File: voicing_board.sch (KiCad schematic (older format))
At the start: 275 parts, among them Q1 MMBT3904, Q14 MMBT3904, Q15 MMBT3904, Q16 MMBT3904, Q17 MMBT3904, Q18 MMBT3904, Q19 MMBT3904, Q2 MMBT3904, Q20 MMBT3904, Q21 MMBT3904, Q22 MMBT3904, Q23 MMBT3904, Q24 MMBT3904, Q25 MMBT3904, Q26 MMBT3904, Q27 MMBT3904, Q28-1 MMBT3904, Q29-1 MMBT3904, Q3 MMBT3904, Q30 MMBT3904, Q31-1 MMBT3904, Q4 MMBT3904, Q5 MMBT3906, Q6 MMBT3906, Q7 MMBT3906, Q8 MMBT3906, Q9 MMBT3904, U1 MC14584, U2 4558, U3 4558, U5 4558, U6-1 4558, U7 4558

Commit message: first commit since importing netlist with updated footprints. Bit of a mess now. Major reroute is in order
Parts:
- C35, C61-1: footprint Capacitors_SMD:c_elec_6.3x5.3 -> Capacitors_SMD:c_elec_5x5.3
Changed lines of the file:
@@
 F 0 "C35" H 9450 9475 50  0000 L CNN
 F 1 "47μ" H 9750 9475 50  0000 L CNN
-F 2 "Capacitors_SMD:c_elec_6.3x5.3" H 9675 9575 60  0001 C CNN
+F 2 "Capacitors_SMD:c_elec_5x5.3" H 9675 9575 60  0001 C CNN
 F 3 "" H 9675 9575 60  0000 C CNN
 	1    9675 9575
@@
 F 0 "C61-1" H 13175 2575 50  0000 L CNN
 F 1 "47μ" H 13175 2500 50  0000 L CNN
-F 2 "Capacitors_SMD:c_elec_6.3x5.3" H 13050 2550 60  0001 C CNN
+F 2 "Capacitors_SMD:c_elec_5x5.3" H 13050 2550 60  0001 C CNN
 F 3 "" H 13050 2550 60  0000 C CNN
 	1    13050 2550

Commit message: epic pcb overhaul for 2.0 has begun. depressing
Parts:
- removed TP22, TP23, TP24, TP25: TEST_POINT, MyModules:TEST_POINT_LOOP_4592, symbol TEST_POINT
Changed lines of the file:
@@
 Text HLabel 1775 750  0    100  Input ~ 0
 COMMON_TRIG
-Text HLabel 1450 3600 0    100  Input ~ 0
+Text HLabel 1450 3500 0    100  Input ~ 0
 CB_TRIG
 Text HLabel 12050 7025 2    100  Output ~ 0
@@
 $EndComp
 $Comp
-L R_US R2-1
-U 1 1 56A1AAD0
-P 7825 2325
-F 0 "R2-1" H 7675 2350 50  0000 C CNN
-F 1 "22K" H 7700 2250 50  0000 C CNN
-F 2 "MyModules:SM0603-R-JRL" H 7825 2325 60  0001 C CNN
-F 3 "" H 7825 2325 60  0000 C CNN
-	1    7825 2325
-	1    0    0    -1
-$EndComp
-$Comp
 L R_US R7-1
 U 1 1 56A1AAD6
@@
 	-1   0    0    1
 $EndComp
-Text HLabel 7675 2125 0    100  Input ~ 0
+Text HLabel 7675 2025 0    100  Input ~ 0
 CH_TRIG
 $Comp
@@
 	-1   0    0    1
 $EndComp
-Text HLabel 9700 2125 0    100  Input ~ 0
+Text HLabel 9700 2025 0    100  Input ~ 0
 OH_TRIG
 $Comp
@@
 	1600 4850 1600 4925
 Connection ~ 1600 4425
-Wire Wire Line
-	1450 3600 1600 3600
 Connection ~ 2075 2800
 Wire Wire Line
@@
 	7825 3375 7825 3450
 Connection ~ 7825 2950
-Wire Wire Line
-	7675 2125 7825 2125
 Connection ~ 8300 1325
 Wire Wire Line
@@
 	9850 3375 9850 3450
 Connection ~ 9850 2950
-Wire Wire Line
-	9700 2125 9850 2125
 Connection ~ 10325 1325
 Wire Wire Line
@@
 	0    1    1    0
 $EndComp
-$Comp
-L TEST_POINT TP22
-U 1 1 56CCF221
-P 1600 3450
-F 0 "TP22" V 1750 3275 100 0000 L CNB
-F 1 "TEST_POINT" H 1600 3505 30  0001 C CNN
-F 2 "MyModules:TEST_POINT_LOOP_4592" H 1600 3450 60  0001 C CNN
-F 3 "" H 1600 3450 60  0000 C CNN
-	1    1600 3450
-	0    -1   -1   0
-$EndComp
-Connection ~ 1600 3600
-$Comp
-L TEST_POINT TP23
-U 1 1 56CD43FC
-P 7825 1975
-F 0 "TP23" V 7825 1600 100 0000 L CNB
-F 1 "TEST_POINT" H 7825 2030 30  0001 C CNN
-F 2 "MyModules:TEST_POINT_LOOP_4592" H 7825 1975 60  0001 C CNN
-F 3 "" H 7825 1975 60  0000 C CNN
-	1    7825 1975
-	0    -1   -1   0
-$EndComp
-$Comp
-L TEST_POINT TP24
-U 1 1 56CD66B0
-P 9850 1975
-F 0 "TP24" V 9850 1600 100 0000 L CNB
-F 1 "TEST_POINT" H 9850 2030 30  0001 C CNN
-F 2 "MyModules:TEST_POINT_LOOP_4592" H 9850 1975 60  0001 C CNN
-F 3 "" H 9850 1975 60  0000 C CNN
-	1    9850 1975
-	0    -1   -1   0
-$EndComp
-Connection ~ 9850 2125
-Connection ~ 7825 2125
-$Comp
-L TEST_POINT TP25
-U 1 1 56CD9E51
-P 13350 8875
-F 0 "TP25" V 13350 8500 100 0000 L CNB
-F 1 "TEST_POINT" H 13350 8930 30  0001 C CNN
-F 2 "MyModules:TEST_POINT_LOOP_4592" H 13350 8875 60  0001 C CNN
-F 3 "" H 13350 8875 60  0000 C CNN
-	1    13350 8875
-	0    -1   -1   0
-$EndComp
-Connection ~ 13350 9025
 Connection ~ 19150 5850
 NoConn ~ 1600 6875
@@
 Text Notes 9750 3750 0    60   ~ 0
 Simulate this OH decay circuit!
+$Comp
+L R_US R2-1
+U 1 1 56A1AAD0
+P 7825 2325
+F 0 "R2-1" H 7675 2350 50  0000 C CNN
+F 1 "22K" H 7700 2250 50  0000 C CNN
+F 2 "MyModules:SM0603-R-JRL" H 7825 2325 60  0001 C CNN
+F 3 "" H 7825 2325 60  0000 C CNN
+	1    7825 2325
+	1    0    0    -1
+$EndComp
+Wire Wire Line
+	7675 2025 7825 2025
+Wire Wire Line
+	7825 2025 7825 2125
+Wire Wire Line
+	9700 2025 9850 2025
+Wire Wire Line
+	9850 2025 9850 2125
+Wire Wire Line
+	1450 3500 1600 3500
+Wire Wire Line
+	1600 3500 1600 3600
 $EndSCHEMATC

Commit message: changed all NPN and PNPs to 945 and 733 respectively
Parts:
- Q1, Q14, Q15, Q16, Q17, Q18, Q19, Q2, Q20, Q21, Q22, Q23, Q24, Q25, Q26, Q27, Q28-1, Q29-1, Q3, Q30, Q31-1, Q4, Q9: value MMBT3904 -> C945; symbol MMBT3904 -> C945
- Q5, Q6, Q7, Q8: value MMBT3906 -> A733; symbol MMBT3906 -> A733
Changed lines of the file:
@@
 $EndComp
 $Comp
-L MMBT3904 Q9
+L C945 Q9
 U 1 1 5693E26E
 P 1850 5950
 F 0 "Q9" H 2075 6150 100 0000 L CNB
-F 1 "MMBT3904" H 1450 5825 50  0001 L CNN
+F 1 "C945" H 1450 5825 50  0001 L CNN
 F 2 "MyModules:SOT23-132-JRL" H 2050 5875 50  0001 L CIN
 F 3 "" H 1850 5950 50  0000 L CNN
@@
 $EndComp
 $Comp
-L MMBT3904 Q15
+L C945 Q15
 U 1 1 5693E2F3
 P 4725 5825
 F 0 "Q15" H 4675 6200 100 0000 L CNB
-F 1 "MMBT3904" H 4325 5700 50  0001 L CNN
+F 1 "C945" H 4325 5700 50  0001 L CNN
 F 2 "MyModules:SOT23-132-JRL" H 4925 5750 50  0001 L CIN
 F 3 "" H 4725 5825 50  0000 L CNN
@@
 $EndComp
 $Comp
-L MMBT3904 Q14
+L C945 Q14
 U 1 1 5693E468
 P 4775 7225
 F 0 "Q14" H 4775 7600 100 0000 L CNB
-F 1 "MMBT3904" H 4375 7100 50  0001 L CNN
+F 1 "C945" H 4375 7100 50  0001 L CNN
 F 2 "MyModules:SOT23-132-JRL" H 4975 7150 50  0001 L CIN
 F 3 "" H 4775 7225 50  0000 L CNN
@@
 CB\nLEVEL
 $Comp
-L MMBT3904 Q1
+L C945 Q1
 U 1 1 5693E582
 P 1975 4425
 F 0 "Q1" H 1800 4675 100 0000 L CNB
-F 1 "MMBT3904" H 1650 4650 50  0001 L CNN
+F 1 "C945" H 1650 4650 50  0001 L CNN
 F 2 "MyModules:SOT23-132-JRL" H 2175 4350 50  0001 L CIN
 F 3 "" H 1975 4425 50  0000 L CNN
@@
 $EndComp
 $Comp
-L MMBT3906 Q5
+L A733 Q5
 U 1 1 5693E589
 P 2375 3425
 F 0 "Q5" H 2575 3225 100 0000 L CNB
-F 1 "MMBT3906" H 2575 3425 50  0001 L CNN
+F 1 "A733" H 2575 3425 50  0001 L CNN
 F 2 "MyModules:SOT23-132-JRL" H 2575 3350 50  0001 L CIN
 F 3 "" H 2375 3425 50  0000 L CNN
@@
 $EndComp
 $Comp
-L MMBT3904 Q17
+L C945 Q17
 U 1 1 5693E686
 P 6125 11800
 F 0 "Q17" H 5800 11525 100 0000 L CNB
-F 1 "MMBT3904" H 5725 11675 50  0001 L CNN
+F 1 "C945" H 5725 11675 50  0001 L CNN
 F 2 "MyModules:SOT23-132-JRL" H 6325 11725 50  0001 L CIN
 F 3 "" H 6125 11800 50  0000 L CNN
@@
 $EndComp
 $Comp
-L MMBT3904 Q16
+L C945 Q16
 U 1 1 5693E6ED
 P 6125 9125
 F 0 "Q16" H 5825 8900 100 0000 L CNB
-F 1 "MMBT3904" H 5725 9000 50  0001 L CNN
+F 1 "C945" H 5725 9000 50  0001 L CNN
 F 2 "MyModules:SOT23-132-JRL" H 6325 9050 50  0001 L CIN
 F 3 "" H 6125 9125 50  0000 L CNN
@@
 $EndComp
 $Comp
-L MMBT3904 Q19
+L C945 Q19
 U 1 1 5693E7B7
 P 10400 9825
 F 0 "Q19" H 10100 9625 100 0000 L CNB
-F 1 "MMBT3904" H 10000 9700 50  0001 L CNN
+F 1 "C945" H 10000 9700 50  0001 L CNN
 F 2 "MyModules:SOT23-132-JRL" H 10600 9750 50  0001 L CIN
 F 3 "" H 10400 9825 50  0000 L CNN
@@
 $EndComp
 $Comp
-L MMBT3904 Q20
+L C945 Q20
 U 1 1 5693E7F3
 P 8550 12325
 F 0 "Q20" H 8275 12550 100 0000 L CNB
-F 1 "MMBT3904" H 8150 12200 50  0001 L CNN
+F 1 "C945" H 8150 12200 50  0001 L CNN
 F 2 "MyModules:SOT23-132-JRL" H 8750 12250 50  0001 L CIN
 F 3 "" H 8550 12325 50  0000 L CNN
@@
 $EndComp
 $Comp
-L MMBT3904 Q25
+L C945 Q25
 U 1 1 569A0C3C
 P 8925 14250
 F 0 "Q25" H 9125 14350 100 0000 L CNB
-F 1 "MMBT3904" H 8525 14125 50  0001 L CNN
+F 1 "C945" H 8525 14125 50  0001 L CNN
 F 2 "MyModules:SOT23-132-JRL" H 9125 14175 50  0001 L CIN
 F 3 "" H 8925 14250 50  0000 L CNN
@@
 $EndComp
 $Comp
-L MMBT3904 Q18
+L C945 Q18
 U 1 1 569A4928
 P 6125 14450
 F 0 "Q18" H 6100 14750 100 0000 L CNB
-F 1 "MMBT3904" H 5725 14325 50  0001 L CNN
+F 1 "C945" H 5725 14325 50  0001 L CNN
 F 2 "MyModules:SOT23-132-JRL" H 6325 14375 50  0001 L CIN
 F 3 "" H 6125 14450 50  0000 L CNN
@@
 CY\nLEVEL
 $Comp
-L MMBT3904 Q2
+L C945 Q2
 U 1 1 569FC4C8
 P 12975 9700
 F 0 "Q2" H 12800 9925 100 0000 L CNB
-F 1 "MMBT3904" H 12650 9925 50  0001 L CNN
+F 1 "C945" H 12650 9925 50  0001 L CNN
 F 2 "MyModules:SOT23-132-JRL" H 13175 9625 50  0001 L CIN
 F 3 "" H 12975 9700 50  0000 L CNN
@@
 $EndComp
 $Comp
-L MMBT3906 Q6
+L A733 Q6
 U 1 1 569FC4CE
 P 12575 8850
 F 0 "Q6" H 12775 8925 100 0000 L CNB
-F 1 "MMBT3906" H 12775 8850 50  0001 L CNN
+F 1 "A733" H 12775 8850 50  0001 L CNN
 F 2 "MyModules:SOT23-132-JRL" H 12775 8775 50  0001 L CIN
 F 3 "" H 12575 8850 50  0000 L CNN
@@
 $EndComp
 $Comp
-L MMBT3904 Q4
+L C945 Q4
 U 1 1 56A1AAB2
 P 8200 2950
 F 0 "Q4" H 8050 2650 100 0000 L CNB
-F 1 "MMBT3904" H 7875 3175 50  0001 L CNN
+F 1 "C945" H 7875 3175 50  0001 L CNN
 F 2 "MyModules:SOT23-132-JRL" H 8400 2875 50  0001 L CIN
 F 3 "" H 8200 2950 50  0000 L CNN
@@
 $EndComp
 $Comp
-L MMBT3906 Q8
+L A733 Q8
 U 1 1 56A1AAB8
 P 8600 1950
 F 0 "Q8" H 8800 1700 100 0000 L CNB
-F 1 "MMBT3906" H 8800 1950 50  0001 L CNN
+F 1 "A733" H 8800 1950 50  0001 L CNN
 F 2 "MyModules:SOT23-132-JRL" H 8800 1875 50  0001 L CIN
 F 3 "" H 8600 1950 50  0000 L CNN
@@
 CH_TRIG
 $Comp
-L MMBT3904 Q3
+L C945 Q3
 U 1 1 56A1B851
 P 10225 2950
 F 0 "Q3" H 10050 2725 100 0000 L CNB
-F 1 "MMBT3904" H 9900 3175 50  0001 L CNN
+F 1 "C945" H 9900 3175 50  0001 L CNN
 F 2 "MyModules:SOT23-132-JRL" H 10425 2875 50  0001 L CIN
 F 3 "" H 10225 2950 50  0000 L CNN
@@
 $EndComp
 $Comp
-L MMBT3906 Q7
+L A733 Q7
 U 1 1 56A1B857
 P 10775 1950
 F 0 "Q7" H 10975 1700 100 0000 L CNB
-F 1 "MMBT3906" H 10975 1950 50  0001 L CNN
+F 1 "A733" H 10975 1950 50  0001 L CNN
 F 2 "MyModules:SOT23-132-JRL" H 10975 1875 50  0001 L CIN
 F 3 "" H 10775 1950 50  0000 L CNN
@@
 $EndComp
 $Comp
-L MMBT3904 Q21
+L C945 Q21
 U 1 1 56A27D2F
 P 10425 4300
 F 0 "Q21" H 10650 4175 100 0000 L CNB
-F 1 "MMBT3904" H 10600 4225 50  0001 L CNN
+F 1 "C945" H 10600 4225 50  0001 L CNN
 F 2 "MyModules:SOT23-132-JRL" H 10625 4225 50  0001 L CIN
 F 3 "" H 10425 4300 50  0000 L CNN
@@
 $EndComp
 $Comp
-L MMBT3904 Q24
+L C945 Q24
 U 1 1 56A41564
 P 11700 2825
 F 0 "Q24" H 11875 3025 100 0000 L CNB
-F 1 "MMBT3904" H 11375 3050 50  0001 L CNN
+F 1 "C945" H 11375 3050 50  0001 L CNN
 F 2 "MyModules:SOT23-132-JRL" H 11900 2750 50  0001 L CIN
 F 3 "" H 11700 2825 50  0000 L CNN
@@
 $EndComp
 $Comp
-L MMBT3904 Q29-1
+L C945 Q29-1
 U 1 1 56A4ABB0
 P 13600 3075
 F 0 "Q29-1" H 13125 2850 100 0000 L CNB
-F 1 "MMBT3904" H 13275 3300 50  0001 L CNN
+F 1 "C945" H 13275 3300 50  0001 L CNN
 F 2 "MyModules:SOT23-132-JRL" H 13800 3000 50  0001 L CIN
 F 3 "" H 13600 3075 50  0000 L CNN
@@
 $EndComp
 $Comp
-L MMBT3904 Q28-1
+L C945 Q28-1
 U 1 1 56A59C33
 P 13600 4875
 F 0 "Q28-1" H 13500 5325 100 0000 L CNB
-F 1 "MMBT3904" H 13275 5100 50  0001 L CNN
+F 1 "C945" H 13275 5100 50  0001 L CNN
 F 2 "MyModules:SOT23-132-JRL" H 13800 4800 50  0001 L CIN
 F 3 "" H 13600 4875 50  0000 L CNN
@@
 $EndComp
 $Comp
-L MMBT3904 Q27
+L C945 Q27
 U 1 1 56A7C339
 P 15125 3550
 F 0 "Q27" H 14800 3325 100 0000 L CNB
-F 1 "MMBT3904" H 14725 3425 50  0001 L CNN
+F 1 "C945" H 14725 3425 50  0001 L CNN
 F 2 "MyModules:SOT23-132-JRL" H 15325 3475 50  0001 L CIN
 F 3 "" H 15125 3550 50  0000 L CNN
@@
 $EndComp
 $Comp
-L MMBT3904 Q26
+L C945 Q26
 U 1 1 5692A116
 P 18050 3350
 F 0 "Q26" H 17750 3600 100 0000 L CNB
-F 1 "MMBT3904" H 17650 3225 50  0001 L CNN
+F 1 "C945" H 17650 3225 50  0001 L CNN
 F 2 "MyModules:SOT23-132-JRL" H 18250 3275 50  0001 L CIN
 F 3 "" H 18050 3350 50  0000 L CNN
@@
 $EndComp
 $Comp
-L MMBT3904 Q30
+L C945 Q30
 U 1 1 5696772B
 P 15125 5725
 F 0 "Q30" H 14700 5375 100 0000 L CNB
-F 1 "MMBT3904" H 14725 5600 50  0001 L CNN
+F 1 "C945" H 14725 5600 50  0001 L CNN
 F 2 "MyModules:SOT23-132-JRL" H 15325 5650 50  0001 L CIN
 F 3 "" H 15125 5725 50  0000 L CNN
@@
 $EndComp
 $Comp
-L MMBT3904 Q31-1
+L C945 Q31-1
 U 1 1 56967795
 P 18050 5525
 F 0 "Q31-1" H 17750 5800 100 0000 L CNB
-F 1 "MMBT3904" H 17650 5400 50  0001 L CNN
+F 1 "C945" H 17650 5400 50  0001 L CNN
 F 2 "MyModules:SOT23-132-JRL" H 18250 5450 50  0001 L CIN
 F 3 "" H 18050 5525 50  0000 L CNN
@@
 Increase C60-1 to compensate\nfor 1meg decay pot instead of 2meg?
 $Comp
-L MMBT3904 Q22
+L C945 Q22
 U 1 1 57A174FA
 P 11600 4300
 F 0 "Q22" H 11325 4025 100 0000 L CNB
-F 1 "MMBT3904" H 11275 4525 50  0001 L CNN
+F 1 "C945" H 11275 4525 50  0001 L CNN
 F 2 "MyModules:SOT23-132-JRL" H 11800 4225 50  0001 L CIN
 F 3 "" H 11600 4300 50  0000 L CNN
@@
 $EndComp
 $Comp
-L MMBT3904 Q23
+L C945 Q23
 U 1 1 57A17F29
 P 12000 4300
 F 0 "Q23" H 11700 4025 100 0000 L CNB
-F 1 "MMBT3904" H 11675 4525 50  0001 L CNN
+F 1 "C945" H 11675 4525 50  0001 L CNN
 F 2 "MyModules:SOT23-132-JRL" H 12200 4225 50  0001 L CIN
 F 3 "" H 12000 4300 50  0000 L CNN

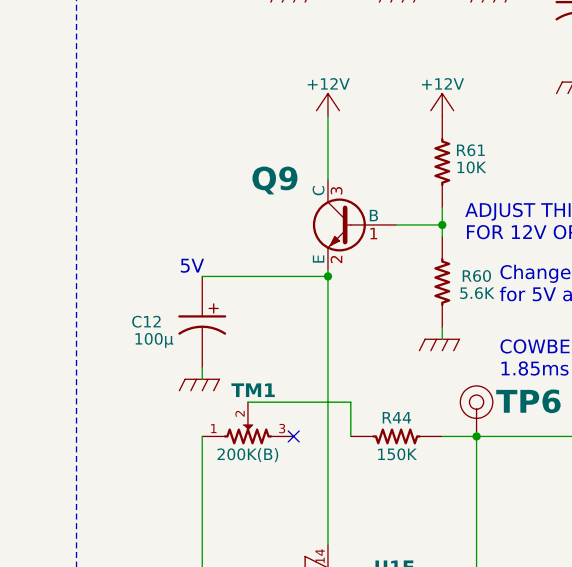
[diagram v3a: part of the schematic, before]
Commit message: more corrections and adjustments based on assembly
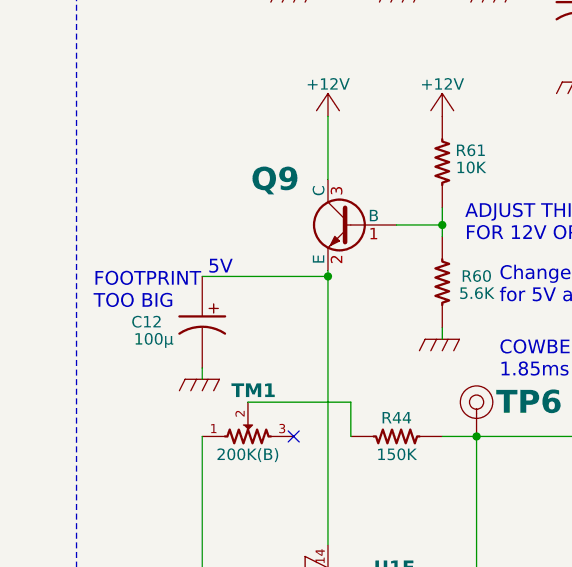
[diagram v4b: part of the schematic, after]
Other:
- note added: "FOOTPRINT \nTOO BIG"
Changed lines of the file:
@@
 	1    0    0    -1
 $EndComp
-Text Notes 1100 6175 0    60   ~ 0
+Text Notes 1225 6175 0    60   ~ 0
 5V
 $Comp
@@
 Wire Wire Line
 	1600 3500 1600 3600
+Text Notes 725  6325 0    60   ~ 0
+FOOTPRINT \nTOO BIG
 $EndSCHEMATC

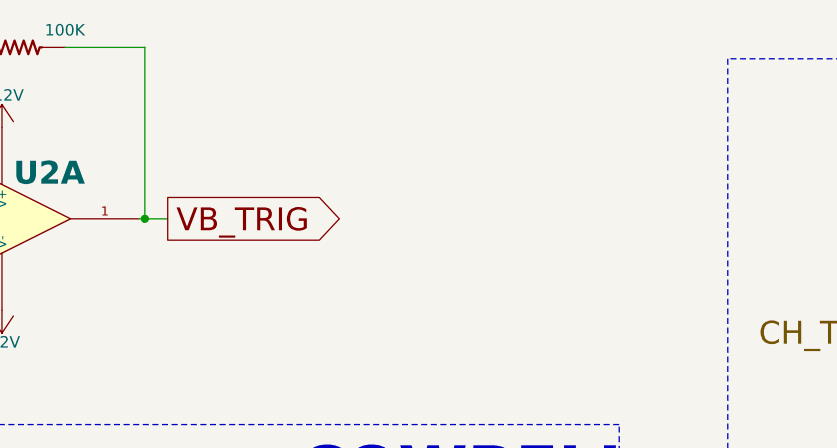
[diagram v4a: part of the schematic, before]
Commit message: made some notes on schematics. added beginnings of OM
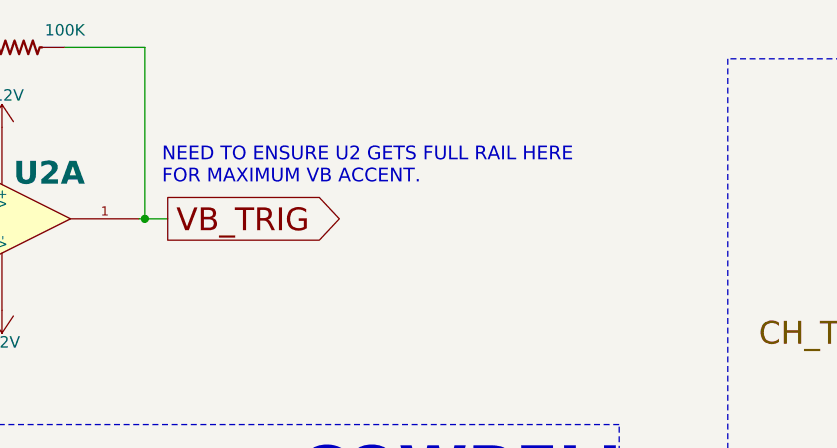
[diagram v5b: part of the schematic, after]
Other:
- note added: "NEED TO ENSURE U2 GETS FULL RAIL HERE \nFOR MAXIMUM VB ACCENT.\n\n"
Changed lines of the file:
@@
 Text Notes 725  6325 0    60   ~ 0
 FOOTPRINT \nTOO BIG
+Text Notes 4350 1475 0    60   ~ 0
+NEED TO ENSURE U2 GETS FULL RAIL HERE \nFOR MAXIMUM VB ACCENT.\n\n
 $EndSCHEMATC
